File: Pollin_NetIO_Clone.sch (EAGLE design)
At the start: 62 parts, among them IC1 7805, IC2 LM317T, IC3 ENC28J60SP, IC4 MAX232, IC5 MEGA32-16PU, J1 MKDSN1,5/2-5,08, J10 MKDSN1,5/2-5,08, J2 74980111212, J3 618025231221, J5 618009231121, J6 MKDSN1,5/2-5,08, J7 MKDSN1,5/2-5,08, J8 MKDSN1,5/2-5,08, J9 MKDSN1,5/2-5,08, Q1 25MHz, Q2 16MHz

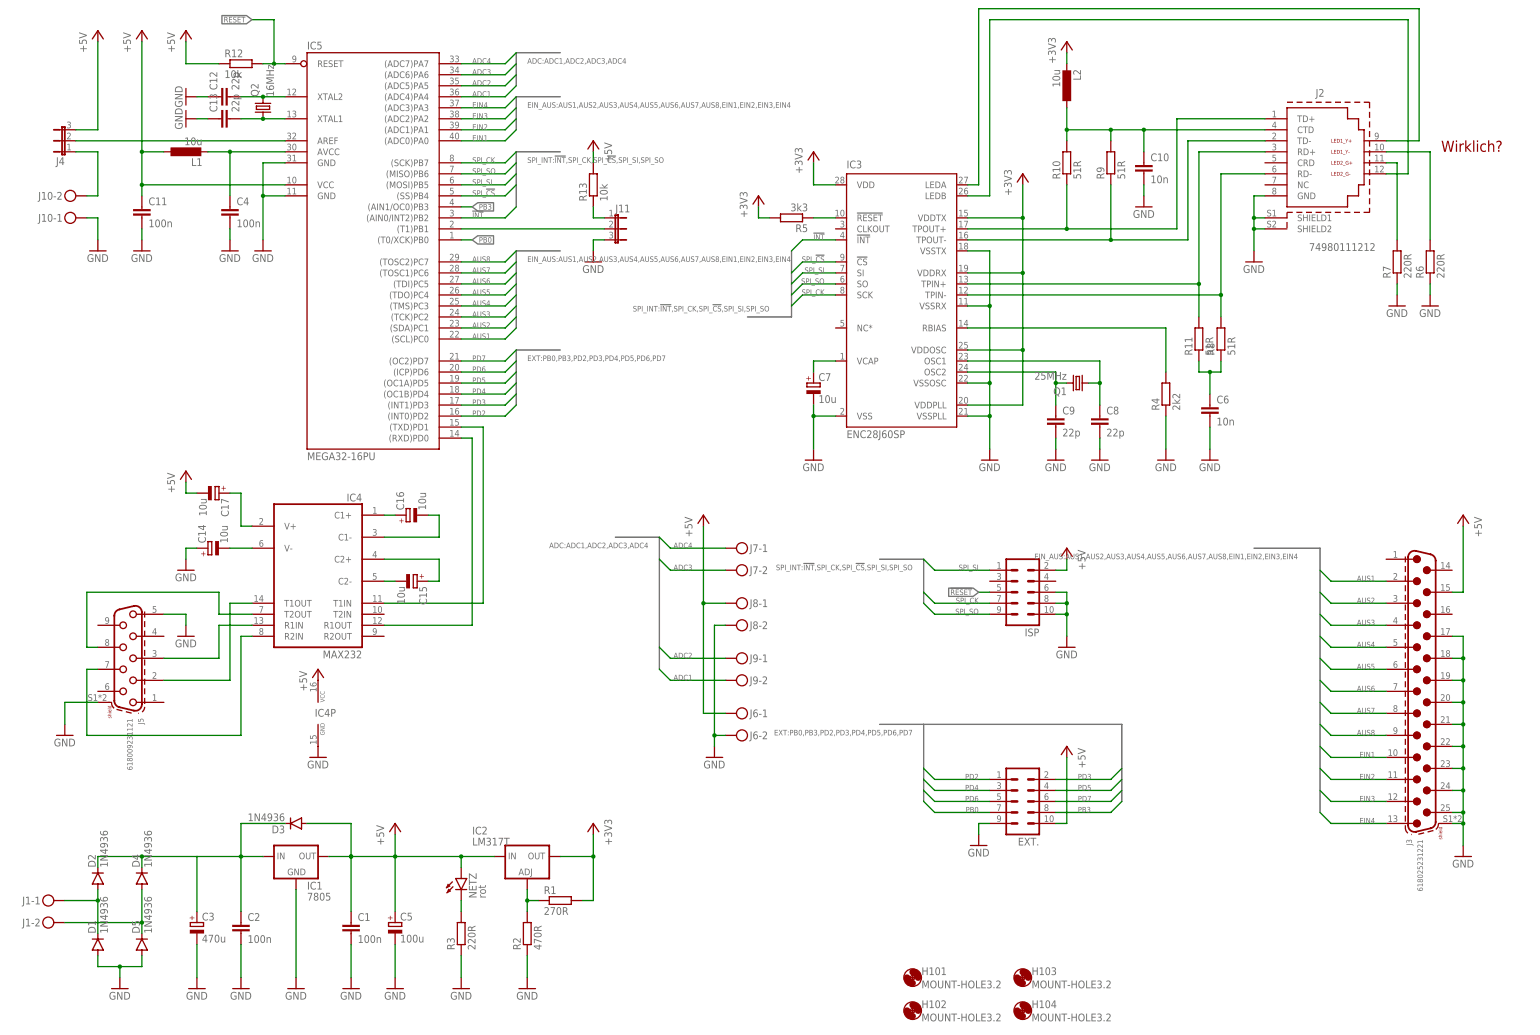
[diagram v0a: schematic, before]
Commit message: * cleanded up schematic * changed RJ45 connector to something compatible with the original one
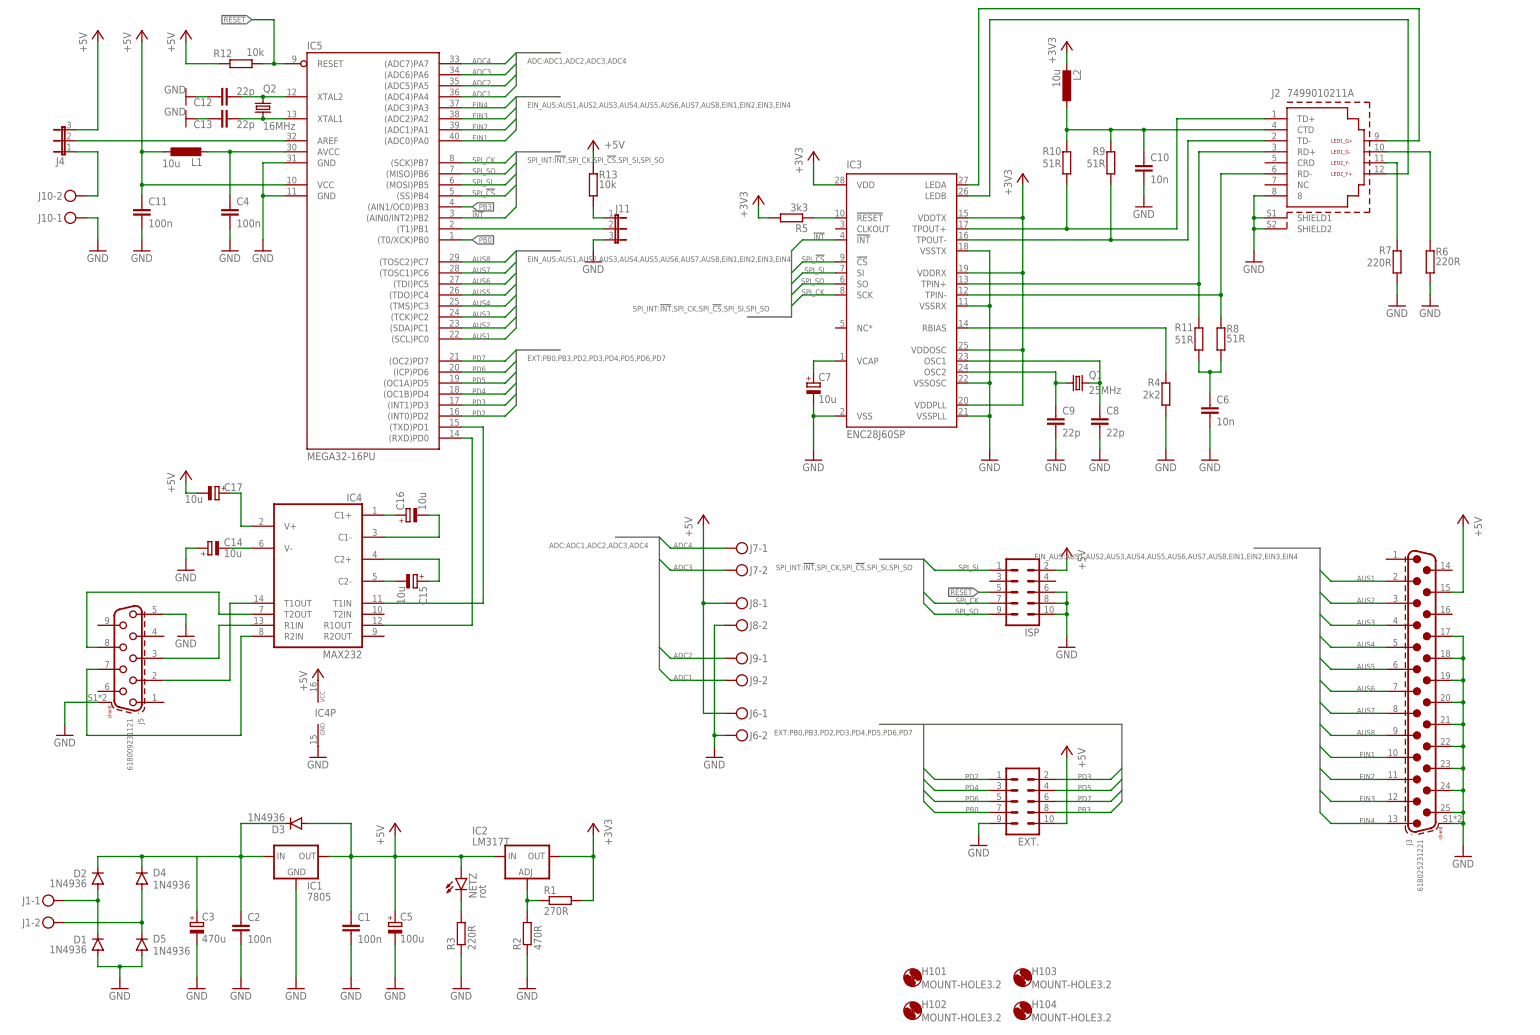
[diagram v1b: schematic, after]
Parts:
- J2: value 74980111212 -> 7499010211A; device Wurth_Signal & Communications_WE-RJ45_LAN:WE-RJ45_74980111212 -> Wurth_Signal & Communications_WE-RJ45_LAN:WE-RJ45_7499010211A
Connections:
- net GND: now also J2.8; no longer J2.GND
- net LEDA: now also J2.LED1_G+; no longer J2.LED1_Y+
- net LEDB: now also J2.LED2_Y+; no longer J2.LED2_G-
- net N$38: now also J2.LED2_Y-; no longer J2.LED2_G+
- net N$39: now also J2.LED1_G-; no longer J2.LED1_Y-
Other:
- note added: "AREF"
- note added: "ext."
- note added: "int."
- note added: "norm"
- note added: "prog"
- note removed: "Wirklich?"

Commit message: * Minor Changes in SCH and BRD * Added original Firmware and EEPROM file * Added STEP model
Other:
- note added: "Original: Trxcom TRJ0011"
